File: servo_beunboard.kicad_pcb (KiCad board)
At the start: 2 copper layers, 16 x 34.8 mm, 13 parts, among them J1 ANGLE_SENSOR, J2 SERVO_INPUT, M1 Motor_DC, U1 DRV8212, U6 SPX5205M5-L-3.3

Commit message: v1
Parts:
- removed ? (x2): , 
- added H1: MountingHole, servo-hacking:JLC_ToolingHole, F.Cu at (96.4, 74.5)
- added H2: MountingHole, servo-hacking:JLC_ToolingHole, F.Cu at (106.4, 48.0)
- C3: value BULK -> 22uF
- moved C1 59.5 mm to (100.5, 55.9)
- moved C2 59.5 mm to (95.0, 55.9)
- moved C3 59.5 mm to (98.9, 52.0)
- moved J1 59.5 mm to (94.7, 49.8)
- moved J2 59.5 mm to (97.9, 47.8)
- moved M1 59.5 mm to (100.9, 70.8)
- moved U1 59.5 mm to (102.8, 63.8)
- moved C4 59.5 mm to (102.0, 60.5)
- moved C5 59.5 mm to (100.3, 63.8)
- moved C7 59.5 mm to (98.3, 63.8)
- moved U6 59.5 mm to (97.7, 55.9)
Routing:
- net VCC: track 39.2 -> 36.2 mm, vias 2 -> 0
- net +3.3V: track 23.0 -> 24.2 mm, vias 0 -> 2

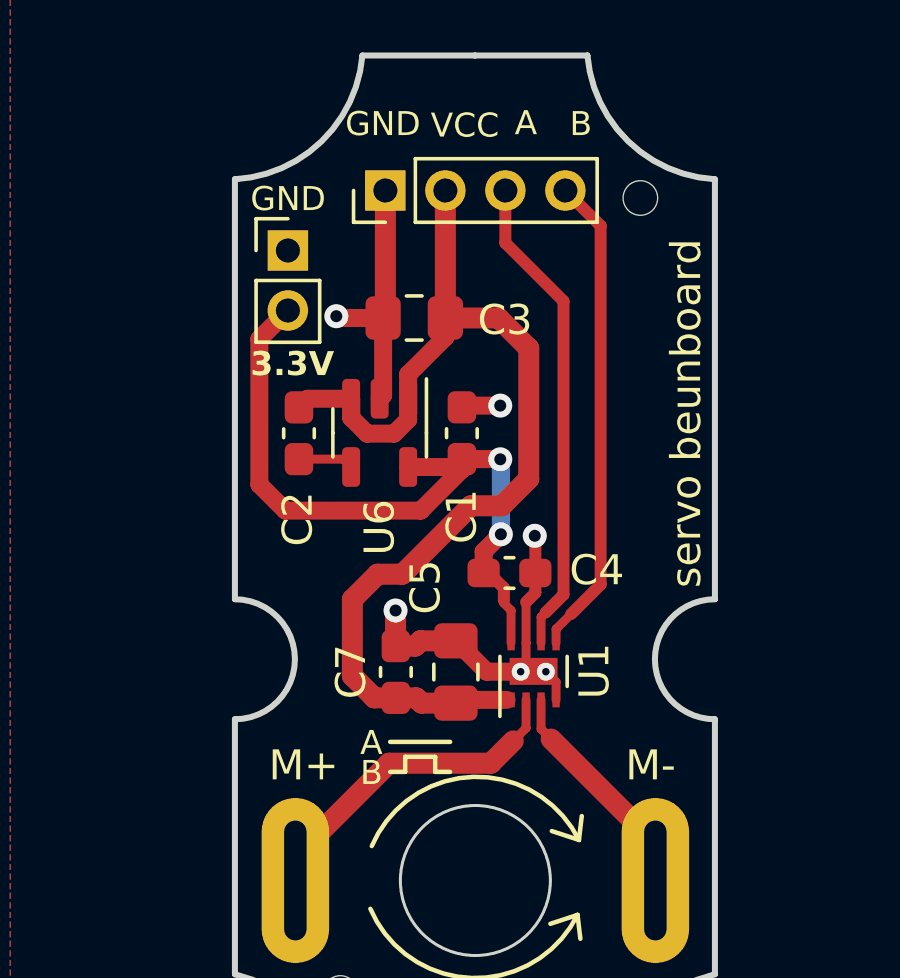
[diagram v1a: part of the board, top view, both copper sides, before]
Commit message: Change LDO JLC part
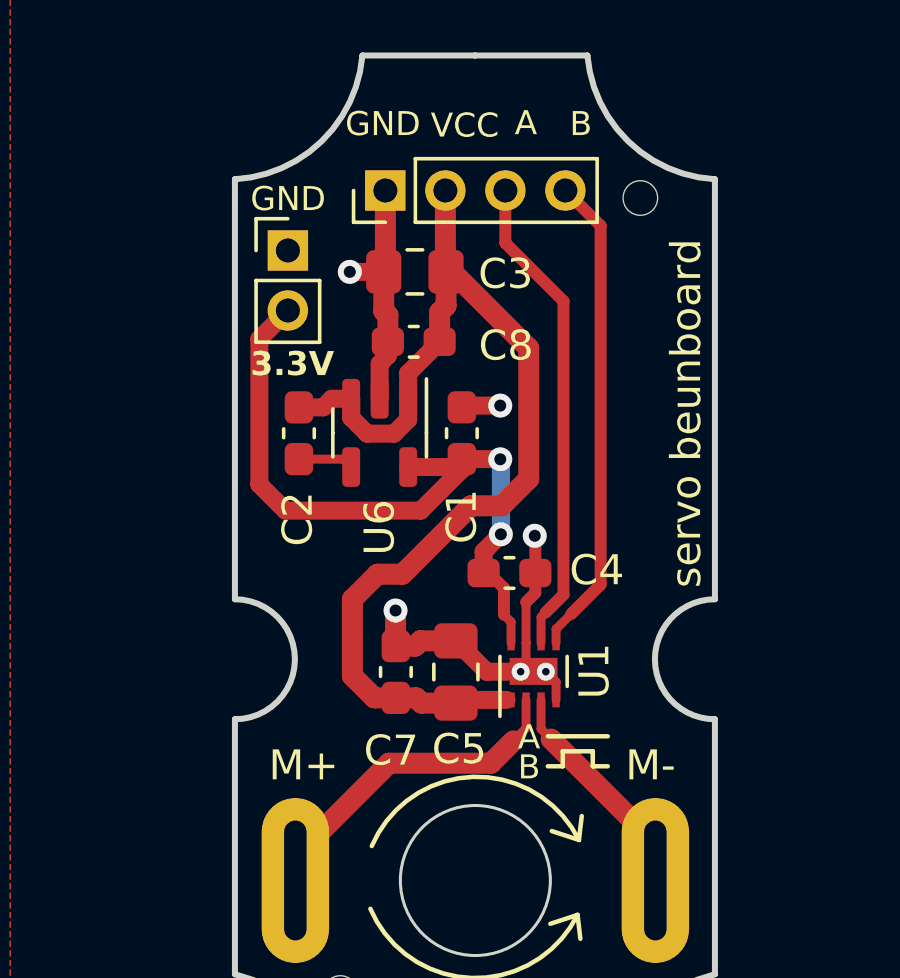
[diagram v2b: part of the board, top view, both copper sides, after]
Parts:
- added C8: 1uF, Capacitor_SMD:C_0603_1608Metric_Pad1.08x0.95mm_HandSolder, F.Cu at (98.9, 52.8)
- U1: value DRV8212 -> DRV8212DSG
- moved C3 1.54 mm to (98.9, 50.5)
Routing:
- net GND: track 22.5 -> 21.7 mm
- net VCC: track 36.2 -> 36.8 mm
